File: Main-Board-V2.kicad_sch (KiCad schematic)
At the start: 5 parts, among them IC1 REG1117-5, J7 776163-5, U11 Teensy4.0

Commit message: Idk what but it is better than before
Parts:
- U11: footprint (none) -> Custom:Teensy40_Raised
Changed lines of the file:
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@@
 			(width 0.254)
 			(type default)
-			(color 0 194 194 1)
+			(color 0 0 194 1)
 		)
 	)
@@
 			(width 0.254)
 			(type default)
-			(color 0 194 194 1)
+			(color 0 0 194 1)
 		)
 	)
@@
 			(width 0.254)
 			(type default)
-			(color 0 194 194 1)
+			(color 0 0 194 1)
 		)
 	)
@@
 			(width 0.254)
 			(type default)
-			(color 0 194 194 1)
+			(color 0 0 194 1)
 		)
 	)
@@
 			(width 0.254)
 			(type default)
-			(color 0 194 194 1)
+			(color 0 0 194 1)
 		)
 	)
@@
 			(width 0.254)
 			(type default)
-			(color 0 194 194 1)
+			(color 0 0 194 1)
 		)
 	)
@@
 			(width 0.254)
 			(type default)
-			(color 0 194 194 1)
+			(color 0 0 194 1)
 		)
 	)
@@
 			(width 0.254)
 			(type default)
-			(color 0 194 194 1)
+			(color 0 0 194 1)
 		)
 	)
@@
 			(width 0.254)
 			(type default)
-			(color 0 194 194 1)
+			(color 0 0 194 1)
 		)
 	)
@@
 			(width 0.254)
 			(type default)
-			(color 0 194 194 1)
+			(color 0 0 194 1)
 		)
 	)
@@
 			(width 0.254)
 			(type default)
-			(color 0 194 194 1)
+			(color 0 0 194 1)
 		)
 	)
@@
 			(width 0.254)
 			(type default)
-			(color 0 194 194 1)
+			(color 0 0 194 1)
 		)
 	)
@@
 			)
 		)
-		(property "Footprint" ""
+		(property "Footprint" "Custom:Teensy40_Raised"
 			(at 193.04 66.04 0)
 			(effects

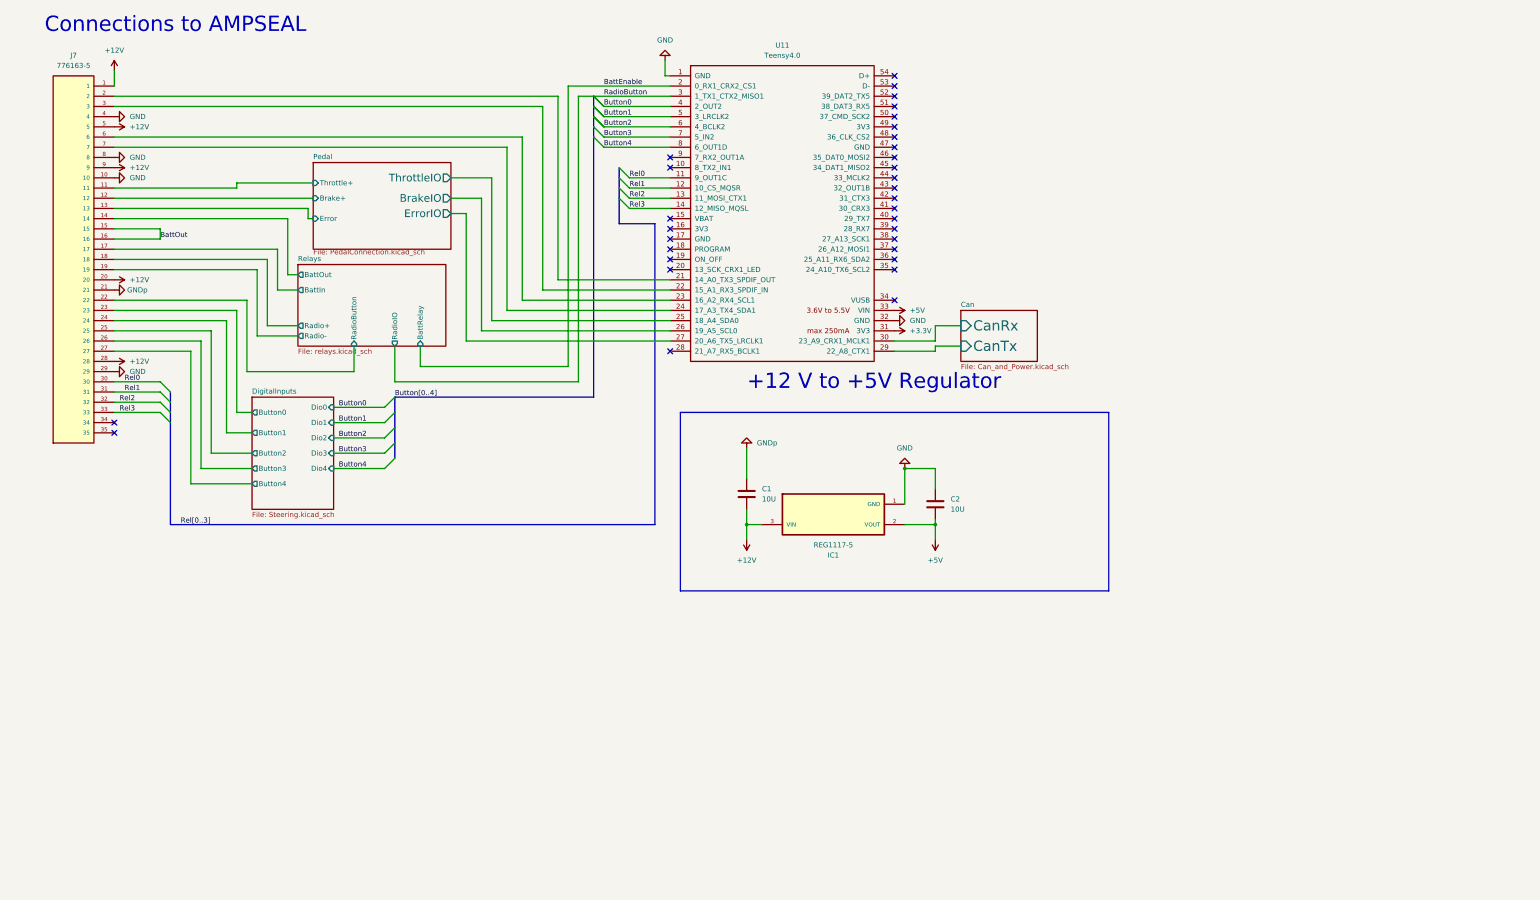
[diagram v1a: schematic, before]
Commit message: made connector match drawing
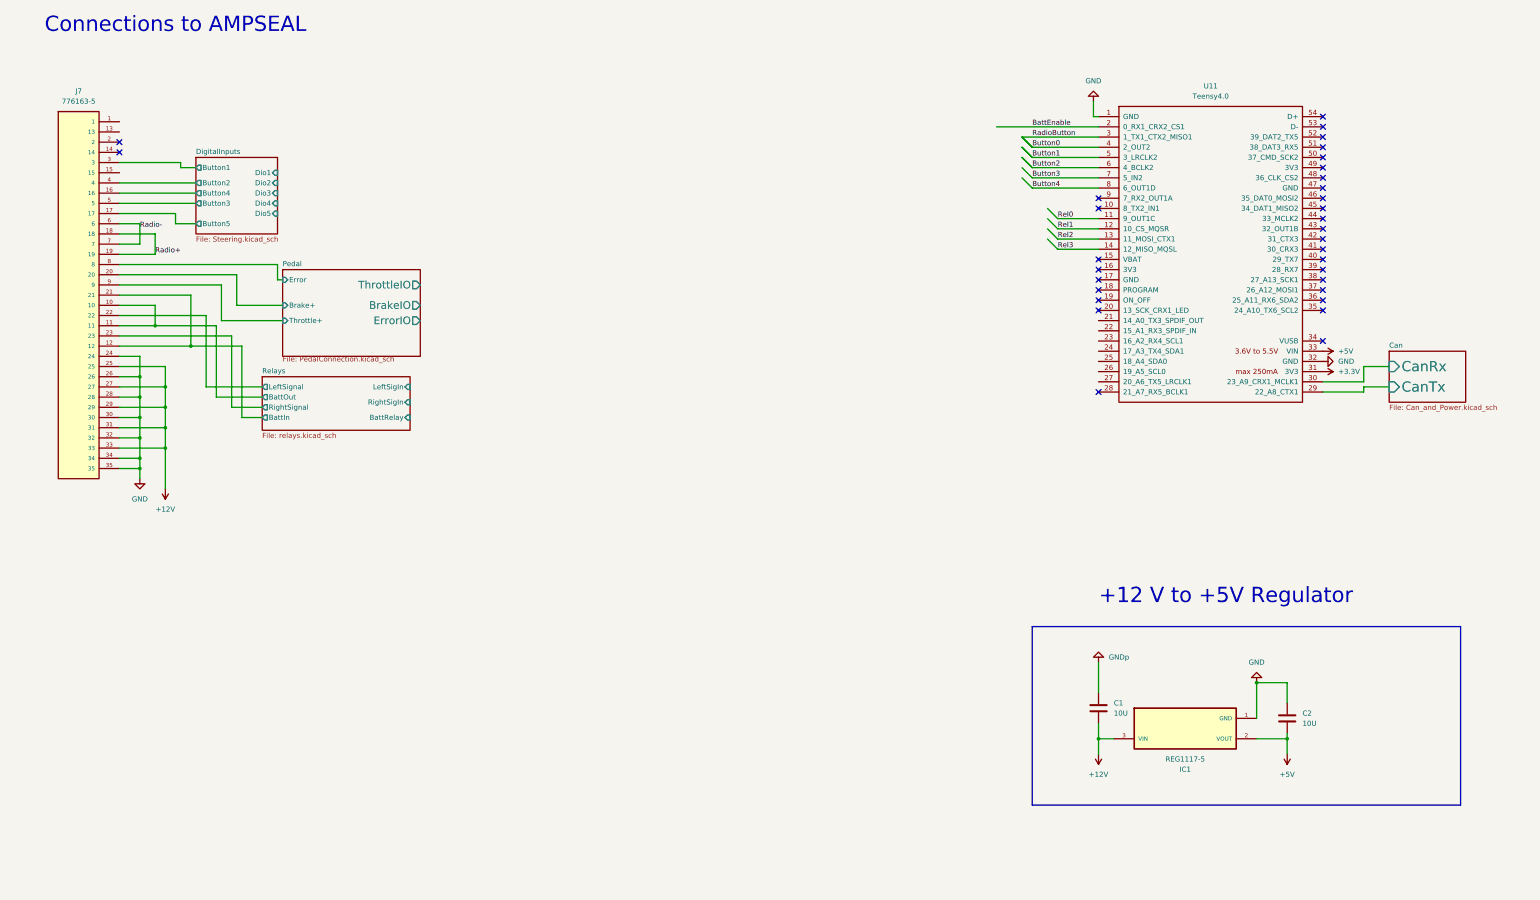
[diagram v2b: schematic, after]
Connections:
- net Relays/Radio- is gone; now on net Radio+: J7.19
- net +12V: now also J7.25, J7.27, J7.29, J7.31, J7.33; no longer J7.1, J7.20, J7.28, J7.5, J7.9
- net DigitalInputs/Button1: now also J7.3; no longer J7.24
- net DigitalInputs/Button2: now also J7.4; no longer J7.25
- net DigitalInputs/Button3: now also J7.5; no longer J7.26
- net DigitalInputs/Button4: now also J7.16; no longer J7.27
- net GND: now also J7.24, J7.26, J7.28, J7.30, J7.32, J7.34, J7.35; no longer J7.10, J7.29, J7.4, J7.8
- net GNDp: no longer J7.21
- net Pedal/Brake+: now also J7.20; no longer J7.12
- net Pedal/BrakeIO: no longer U11.26 (19_A5_SCL0)
- net Pedal/Error: now also J7.8; no longer J7.13
- net Pedal/ErrorIO: no longer U11.27 (20_A6_TX5_LRCLK1)
- net Pedal/Throttle+: now also J7.9; no longer J7.11
- net Pedal/ThrottleIO: no longer U11.25 (18_A4_SDA0)
- net Rel0: no longer J7.30
- net Rel1: no longer J7.31
- net Rel2: no longer J7.32
- net Rel3: no longer J7.33
- net Relays/BattIn: now also J7.12, J7.21; no longer J7.17
- net Relays/BattOut: now also J7.10, J7.11; no longer J7.14
- net at J7.2: no longer U11.21 (14_A0_TX3_SPDIF_OUT)
- net at U11.22 (15_A1_RX3_SPDIF_IN): no longer J7.3
- net at U11.23 (16_A2_RX4_SCL1): no longer J7.6
- net at U11.24 (17_A3_TX4_SDA1): no longer J7.7
- net BattOut: no longer names the net of J7.15
- net BattOut: no longer J7.16
- net DigitalInputs/Button0 renamed Relays/RightSignal
- net Relays/Radio+ renamed Radio+
- net Relays/RadioButton renamed Relays/LeftSignal
- new net DigitalInputs/Button5: J7.17
- new net Radio-: J7.6, J7.7
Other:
- sheet DigitalInputs ports: added Button5, Dio5; removed Button0, Dio0
- sheet Relays ports: added LeftSigIn, LeftSignal, RightSigIn, RightSignal; removed Radio+, Radio-, RadioButton, RadioIO
- moved on the sheet: C1, C2, IC1, J7, U11

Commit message: placed most components
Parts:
- removed J7: 776163-5, 776163-5:TE_776163-5, symbol 776163-5:776163-5
- added C1: 1N, symbol Device:C
- added J4: 1-776231-4, 1-776231-4:TE_1-776231-4, symbol 1-776231-4:1-776231-4
- added R1, R2, R3, R4, R5: R_US, Resistor_SMD:R_0805_2012Metric, symbol Device:R_US
- added U1: OPA325IDBVR, OPA325IDBVR:SOT95P280X145-5N, symbol OPA325IDBVR:OPA325IDBVR
- renumbered C1 to C2, C2 to C3, U11 to U2
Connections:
- net +12V: now also J4.25, J4.27, J4.29, J4.31, J4.33
- net +3.3V: now also U1.5 (V+)
- net DigitalInputs/Button1: now also J4.3
- net DigitalInputs/Button2: now also J4.4
- net DigitalInputs/Button3: now also J4.5
- net DigitalInputs/Button4: now also J4.16
- net DigitalInputs/Button5: now also J4.17
- net GND: now also C1.2, J4.24, J4.26, J4.28, J4.30, J4.32, J4.34, J4.35, R1.2, R3.1, R4.1, U1.2 (V-), U1.4 (-IN)
- net Pedal/Brake+: now also J4.20
- net Pedal/Error: now also J4.8
- net Pedal/Throttle+: now also J4.9
- net Radio+: now also J4.18, J4.19
- net Radio-: now also J4.6, J4.7
- net Relays/BattIn: now also J4.12
- net Relays/BattOut: now also J4.21
- net Relays/LeftSignal: now also J4.22
- net Relays/RightSignal: now also J4.23
- new net: R4.2, R5.1, U1.1 (OUT)
- new net: R2.2, R3.2, U1.3 (+IN)
- new net BattThrotOut: J4.10, J4.11
- new net Encoder: J4.15, R1.1, R2.1
- new net EncoderIO: C1.1, R5.2
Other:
- note added: "Steering Encoder"

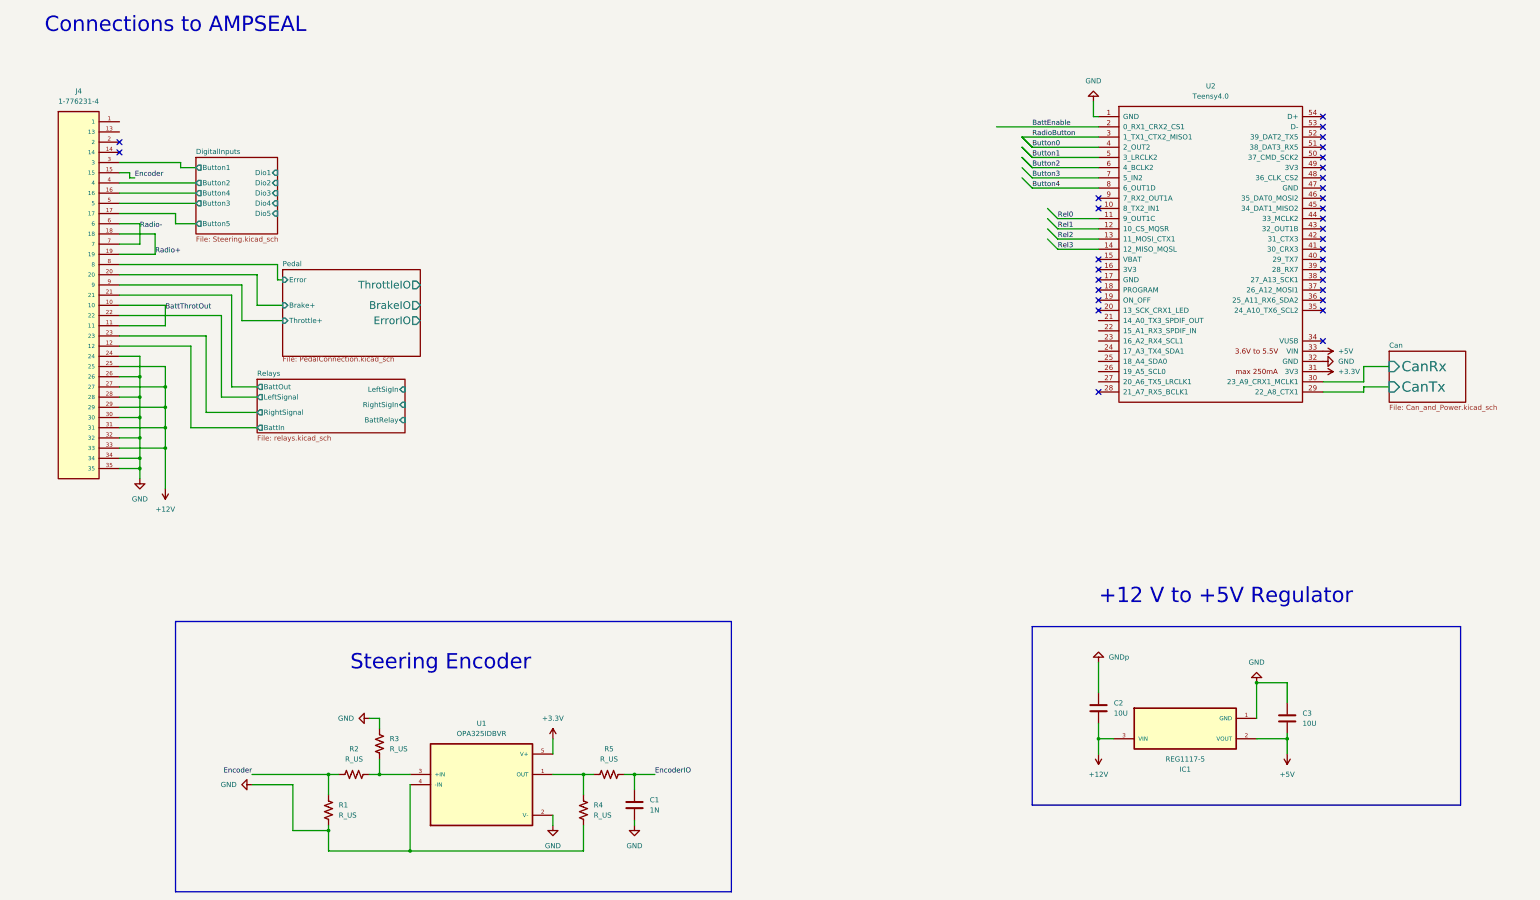
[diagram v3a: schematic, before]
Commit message: replaced CAN chip, power planes
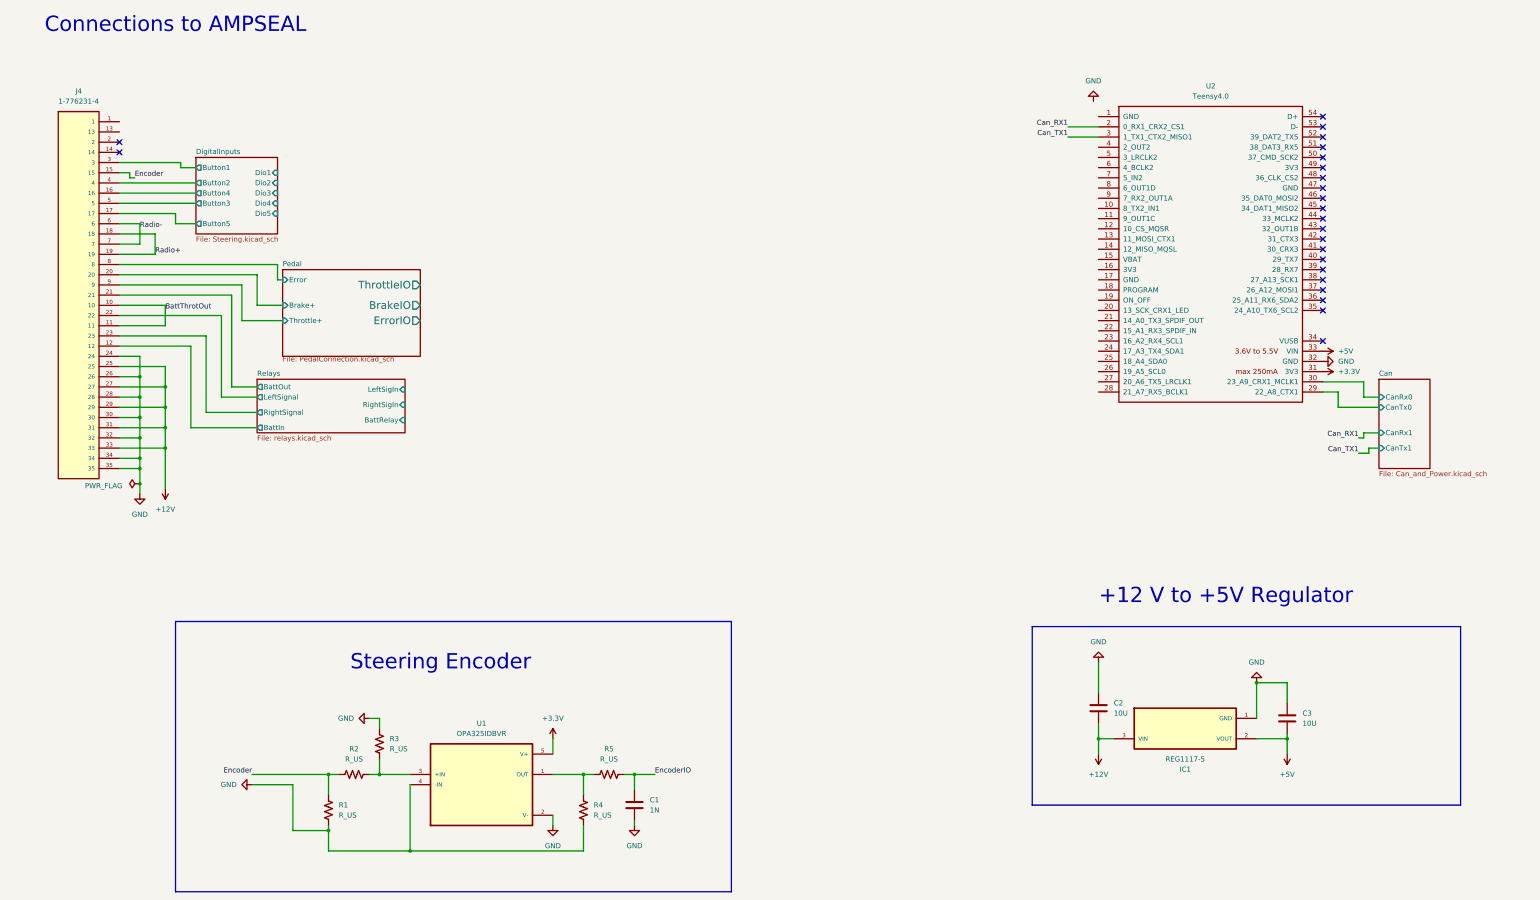
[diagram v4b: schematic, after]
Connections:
- net GNDp is gone; now on net GND: C2.1
- net GND: no longer U2.1 (GND)
- net BattEnable renamed Can_RX1
- net Button0: no longer names the net of U2.4 (2_OUT2)
- net Button1: no longer names the net of U2.5 (3_LRCLK2)
- net Button2: no longer names the net of U2.6 (4_BCLK2)
- net Button3: no longer names the net of U2.7 (5_IN2)
- net Button4: no longer names the net of U2.8 (6_OUT1D)
- net Can/CanRx renamed Can/CanRx0
- net Can/CanTx renamed Can/CanTx0
- net RadioButton renamed Can_TX1
- net Rel0: no longer names the net of U2.11 (9_OUT1C)
- net Rel1: no longer names the net of U2.12 (10_CS_MQSR)
- net Rel2: no longer names the net of U2.13 (11_MOSI_CTX1)
- net Rel3: no longer names the net of U2.14 (12_MISO_MQSL)
- no-connect marks 32 -> 23
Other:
- sheet Can ports: added CanRx0, CanRx1, CanTx0, CanTx1; removed CanRx, CanTx

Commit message: Finished routing
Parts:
- U2: footprint Custom:Teensy40_Raised -> teensy.pretty-master:Teensy40_SMT
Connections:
- net EncoderIO: now also U2.26 (19_A5_SCL0)
- net GND: now also U2.1 (GND)
- net Pedal/BrakeIO: now also U2.27 (20_A6_TX5_LRCLK1)
- net Pedal/ThrottleIO: now also U2.28 (21_A7_RX5_BCLK1)
- net USART_RX: now reaches J4.1
- net USART_RX: now also U2.23 (16_A2_RX4_SCL1)
- net USART_TX: now reaches J4.13
- net USART_TX: now also U2.24 (17_A3_TX4_SDA1)
- net Dio2: now reaches U2.10 (8_TX2_IN1)
- net Dio3: now reaches U2.11 (9_OUT1C)
- net ErrorIO: now reaches U2.12 (10_CS_MQSR)
- net BattRelay: now reaches U2.4 (2_OUT2)
- net LeftSignalIO: now reaches U2.5 (3_LRCLK2)
- net RightSignalIO: now reaches U2.6 (4_BCLK2)
- net Dio5: now reaches U2.7 (5_IN2)
- net Dio4: now reaches U2.8 (6_OUT1D)
- net Dio1: now reaches U2.9 (7_RX2_OUT1A)
- no-connect marks 23 -> 32
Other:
- moved on the sheet: U2

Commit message: Finalized analog components. Everything is done 🙏
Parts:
- C1: footprint (none) -> Capacitor_SMD:C_0805_2012Metric
- C2, C3: footprint Cap10U:CAPC2012X145N -> Capacitor_SMD:C_0805_2012Metric
- R1: value R_US -> 100R
- R2, R3, R4: value R_US -> 10k
- R5: value R_US -> 1k
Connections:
- no-connect marks 32 -> 34
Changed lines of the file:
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@@
 	)
 	(no_connect
+		(at 179.07 83.82)
+	)
+	(no_connect
 		(at 234.95 96.52)
 	)
@@
 	)
 	(no_connect
+		(at 179.07 81.28)
+	)
+	(no_connect
 		(at 179.07 99.06)
 	)
@@
 			)
 		)
-		(property "Footprint" "Cap10U:CAPC2012X145N"
+		(property "Footprint" "Capacitor_SMD:C_0805_2012Metric"
 			(at 282.9052 198.12 0)
 			(effects
@@
 			)
 		)
-		(property "Value" "R_US"
+		(property "Value" "100R"
 			(at 92.71 220.9799 0)
 			(effects
@@
 			)
 		)
-		(property "Footprint" ""
+		(property "Footprint" "Capacitor_SMD:C_0805_2012Metric"
 			(at 167.3352 222.25 0)
 			(effects
@@
 			)
 		)
-		(property "Value" "R_US"
+		(property "Value" "10k"
 			(at 96.52 207.01 90)
 			(effects
@@
 			)
 		)
-		(property "Value" "R_US"
+		(property "Value" "1k"
 			(at 160.02 207.01 90)
 			(effects
@@
 			)
 		)
-		(property "Value" "R_US"
+		(property "Value" "10k"
 			(at 105.41 204.4699 0)
 			(effects
@@
 			)
 		)
-		(property "Value" "R_US"
+		(property "Value" "10k"
 			(at 156.21 220.9799 0)
 			(effects
@@
 			)
 		)
-		(property "Footprint" "Cap10U:CAPC2012X145N"
+		(property "Footprint" "Capacitor_SMD:C_0805_2012Metric"
 			(at 329.8952 200.66 0)
 			(effects

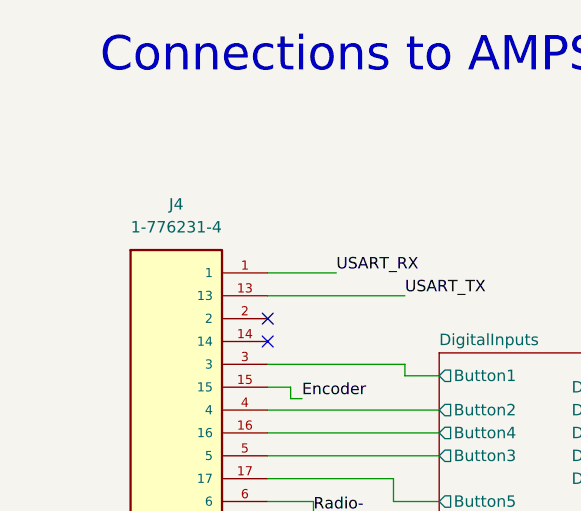
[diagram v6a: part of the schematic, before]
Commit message: Added fuse, switch to horizontal connecotor, redid all routing
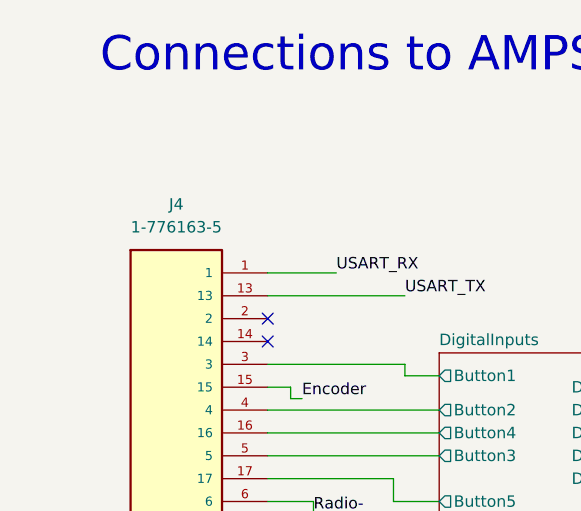
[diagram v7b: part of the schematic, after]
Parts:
- J4: value 1-776231-4 -> 1-776163-5; footprint 1-776231-4:TE_1-776231-4 -> 776163-5:TE_776163-5; Comment 1-776231-4 -> 1-776163-5; MP 1-776231-4 -> 1-776163-5
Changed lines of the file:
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@@
 			)
 		)
-		(property "Value" "1-776231-4"
+		(property "Value" "1-776163-5"
 			(at 27.94 43.18 0)
 			(effects
@@
 			)
 		)
-		(property "Footprint" "1-776231-4:TE_1-776231-4"
+		(property "Footprint" "776163-5:TE_776163-5"
 			(at 27.94 92.71 0)
 			(effects
@@
 			)
 		)
-		(property "Comment" "1-776231-4"
+		(property "Comment" "1-776163-5"
 			(at 27.94 92.71 0)
 			(effects
@@
 			)
 		)
-		(property "MP" "1-776231-4"
+		(property "MP" "1-776163-5"
 			(at 27.94 92.71 0)
 			(effects
